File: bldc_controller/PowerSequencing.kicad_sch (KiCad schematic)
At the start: 0 parts

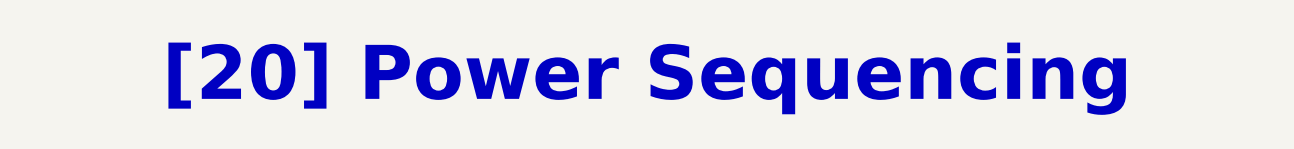
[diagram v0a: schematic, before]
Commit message: Replaced 3v3 buck with WSON package alternative. Will back-annotate components
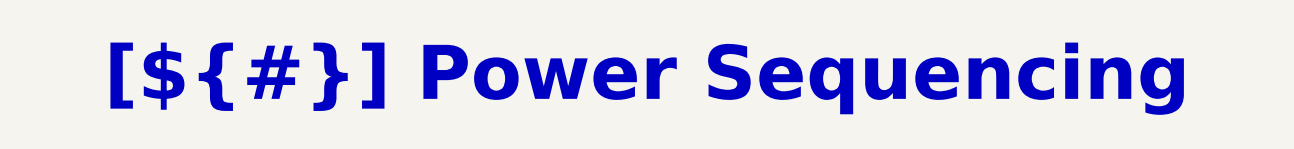
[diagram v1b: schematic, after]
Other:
- company: EPFL Xplore -> ${COMPANY}
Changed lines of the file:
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@@
   (title_block
     (title "Power Sequencing")
-    (rev "1.0")
-    (company "EPFL Xplore")
-    (comment 3 "Author: Vincent Nguyen")
+    (rev "${REVISION}")
+    (company "${COMPANY}")
+    (comment 3 "Author: ${AUTHOR}")
   )
-  (text_box "[20] Power Sequencing"
+  (text_box "[${#}] ${TITLE}"
     (at 80.01 16.51 0) (size 137.16 12.7)
     (stroke (width -0.0001) (type default))
